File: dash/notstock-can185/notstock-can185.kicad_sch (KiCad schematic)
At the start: 27 parts, among them J1 OBD 12V GND H L, J2 LCD-1.85 header, U1 LMR16006YDDCR, U2 TJA1051T/3

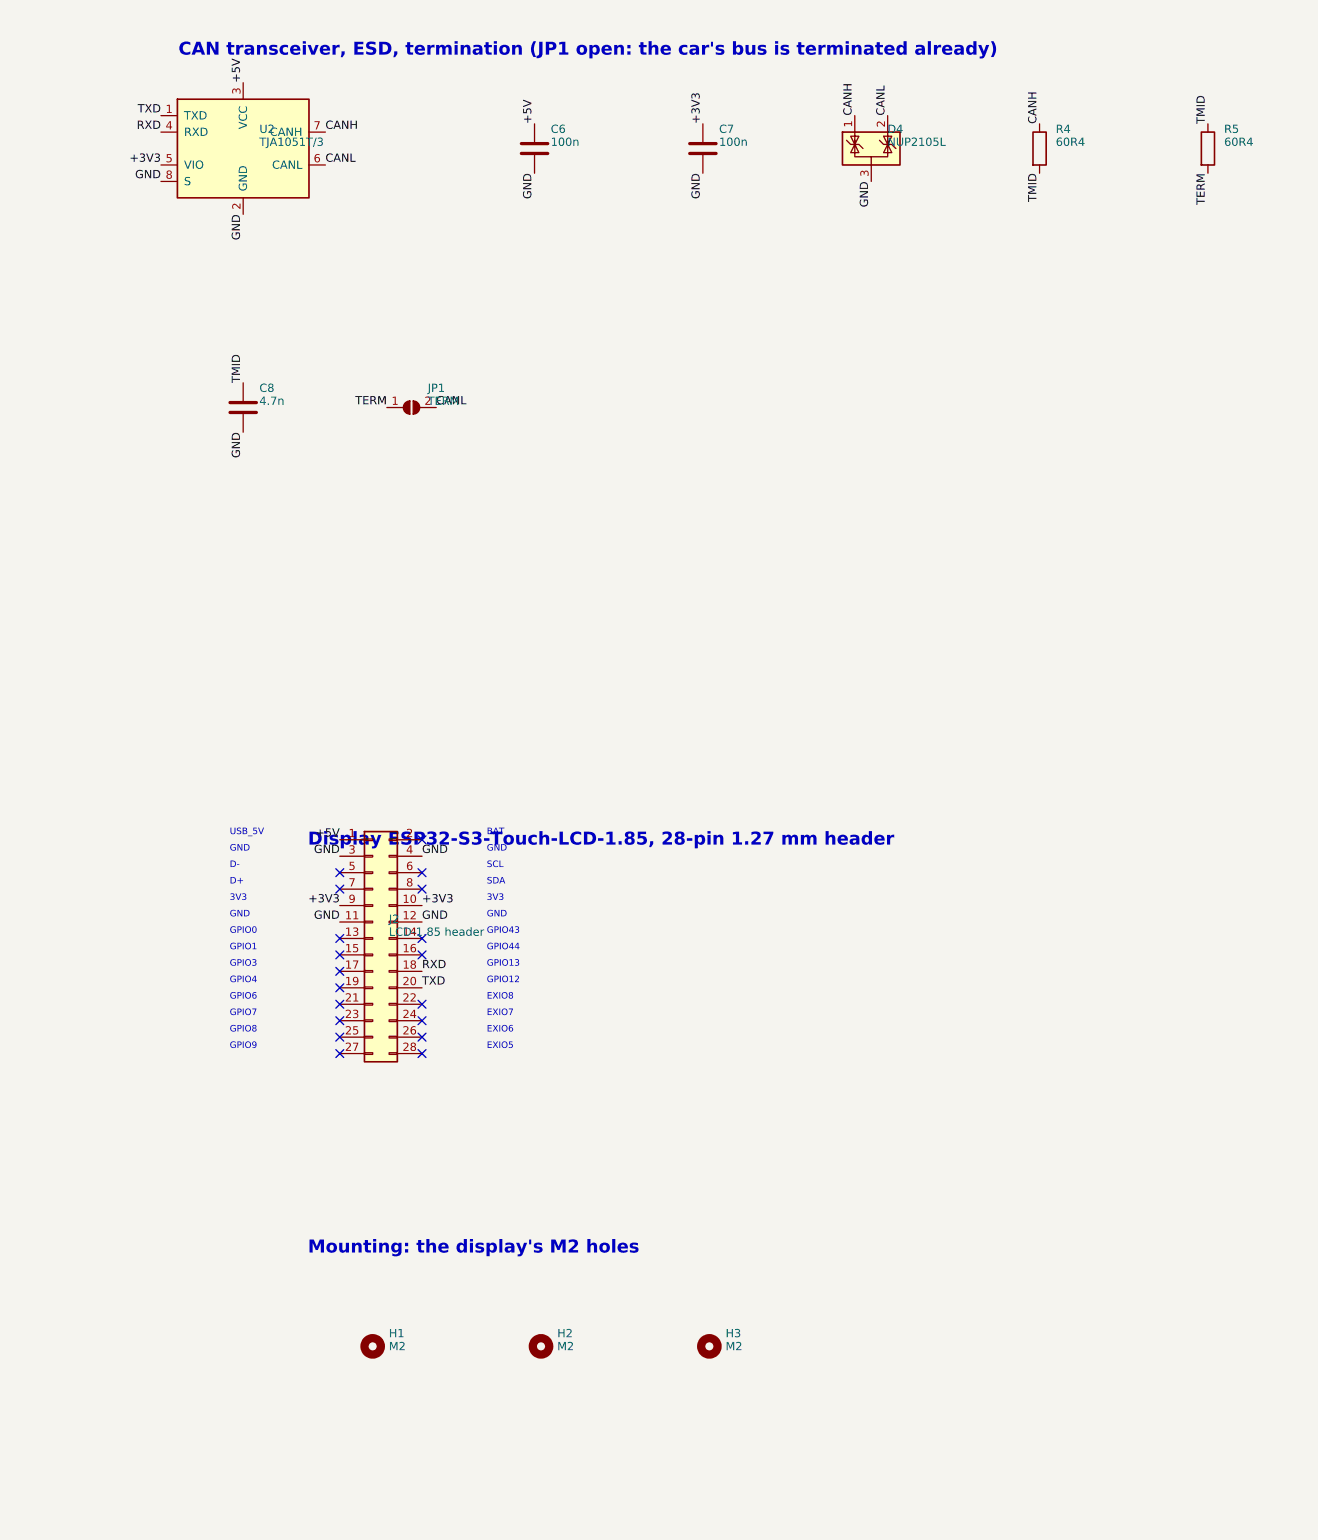
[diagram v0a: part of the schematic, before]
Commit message: CAN 1.85 rev 2: the real ESP32-S3-Touch-LCD-1.85's mechanics and sockets
Waveshare's drawing and schematic of the board (ESP32-S3-LCD-1.85) show
no plug-on header: rev 1 followed the 1.85C, which has one. Now:
Ø48 outline and the three M2 holes from the drawing (DXF), CAN through the
display's 4-pin 1.0 mm UART socket on a 1:1 JST SH cable (GPIO44 TX,
GPIO43 RX, 3V3, GND; 1 k in RXD against the boot ROM's output on
GPIO43), 5 V to the display's USB-C from a USB-C socket on this board.
Edge keepout for the autorouter. DRC clean.

Firmware for the 1.85: CAN on GPIO44/43, the boot loader quiet; the
touch's GPIO1/3 noted as this board's.

Co-Authored-By: Claude Opus 5.5 <noreply@anthropic.com>
Claude-Session: https://claude.ai/code/session_018SKN4tJhAPpVCWtvRZgZpD
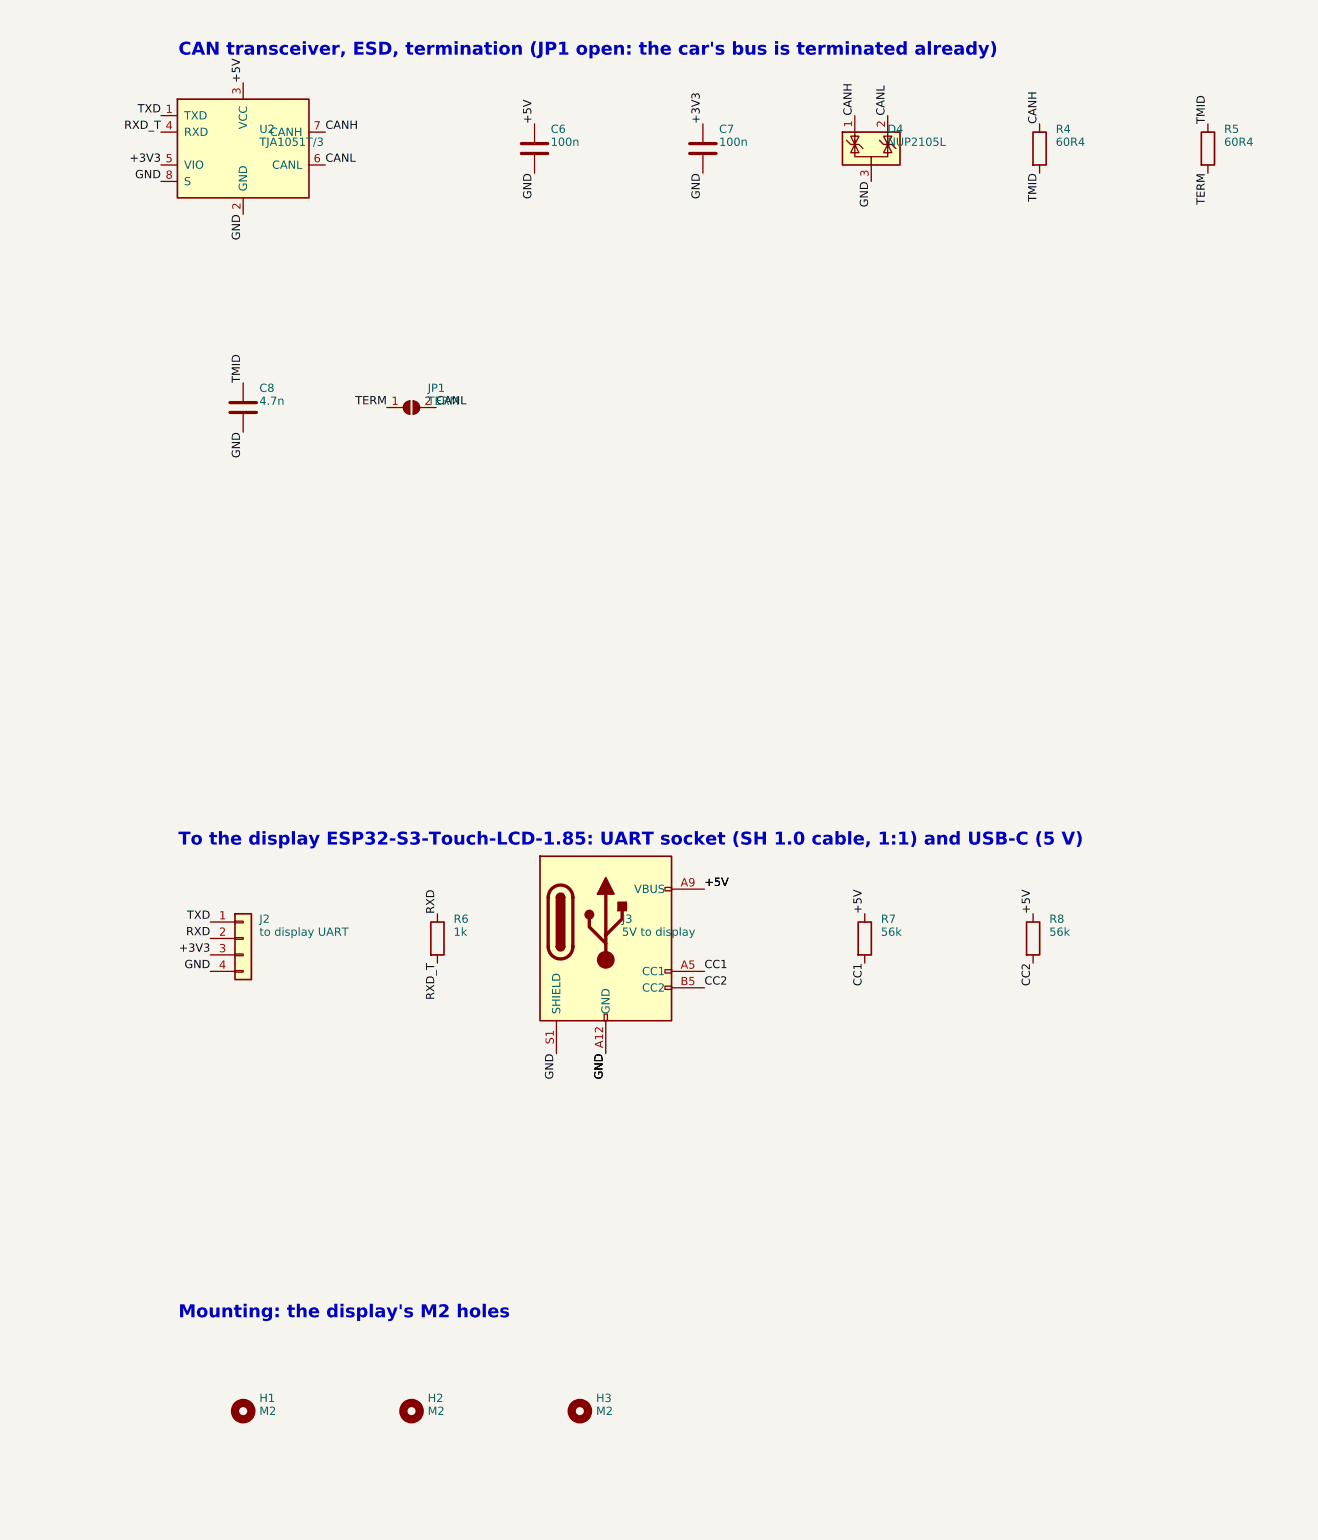
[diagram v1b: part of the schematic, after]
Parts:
- added J3: 5V to display, Connector_USB:USB_C_Receptacle_GCT_USB4125-xx-x_6P_TopMnt_Horizontal, symbol Connector:USB_C_Receptacle_PowerOnly_6P
- added R6: 1k, Resistor_SMD:R_0603_1608Metric, symbol Device:R
- added R7, R8: 56k, Resistor_SMD:R_0603_1608Metric, symbol Device:R
- J2: value LCD-1.85 header -> to display UART; footprint Connector_PinSocket_1.27mm:PinSocket_2x14_P1.27mm_Vertical -> Connector_JST:JST_SH_BM04B-SRSS-TB_1x04-1MP_P1.00mm_Vertical; symbol Connector_Generic:Conn_02x14_Odd_Even -> Connector_Generic:Conn_01x04
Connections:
- net +3V3: now also J2.3 (Pin_3); no longer J2.10 (Pin_10), J2.9 (Pin_9)
- net +5V: now also J3.A9 (VBUS), J3.B9 (VBUS), R7.1, R8.1; no longer J2.1 (Pin_1)
- net GND: now also J3.A12 (GND), J3.B12 (GND), J3.S1 (SHIELD); no longer J2.11 (Pin_11), J2.12 (Pin_12), J2.3 (Pin_3)
- net RXD: now also J2.2 (Pin_2), R6.1; no longer J2.18 (Pin_18), U2.4 (RXD)
- net TXD: now also J2.1 (Pin_1); no longer J2.20 (Pin_20)
- new net CC1: J3.A5 (CC1), R7.2
- new net CC2: J3.B5 (CC2), R8.2
- new net RXD_T: R6.2, U2.4 (RXD)
- no-connect marks 19 -> 0
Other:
- note added: "To the display ESP32-S3-Touch-LCD-1.85: UART socket (SH 1.0 cable, 1:1) and USB-C (5 V)"
- note removed: "3V3"
- note removed: "BAT"
- note removed: "D+"
- note removed: "D-"
- note removed: "Display ESP32-S3-Touch-LCD-1.85, 28-pin 1.27 mm header"
- note removed: "EXIO5"
- note removed: "EXIO6"
- note removed: "EXIO7"
- note removed: "EXIO8"
- note removed: "GND"
- note removed: "GPIO0"
- note removed: "GPIO1"
- note removed: "GPIO12"
- note removed: "GPIO13"
- note removed: "GPIO3"
- note removed: "GPIO4"
- note removed: "GPIO43"
- note removed: "GPIO44"
- note removed: "GPIO6"
- note removed: "GPIO7"
- note removed: "GPIO8"
- note removed: "GPIO9"
- note removed: "SCL"
- note removed: "SDA"
- note removed: "USB_5V"
- moved on the sheet: H1, H2, H3

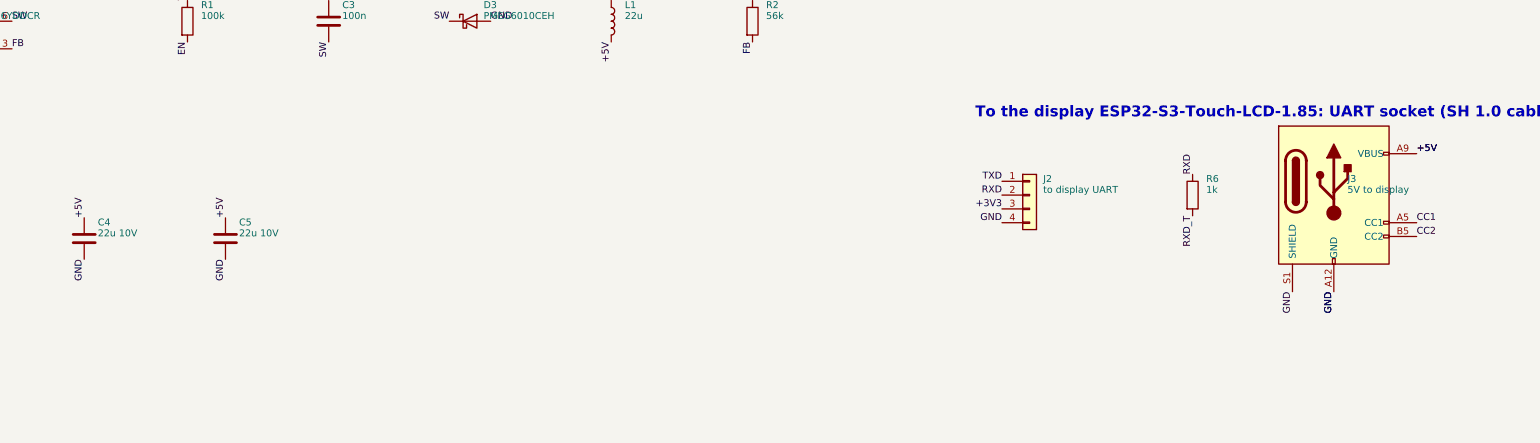
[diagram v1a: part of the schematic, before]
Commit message: CAN 1.85 rev 3: ready for JLCPCB assembly
LCSC numbers for every part (looked up on LCSC/JLCPCB), in design.py,
the schematic (LCSC and MPN fields), the footprints and fab/bom.csv;
values matched to the parts (22 uF 16 V). J3 now the HRO TYPE-C-31-M-12
JLCPCB stocks; its two VBUS pad pairs joined by a short bridge
underneath before autorouting (and routes coming back from the session
not duplicated). Silkscreen past the edge trimmed. DRC clean.

Co-Authored-By: Claude Opus 5.5 <noreply@anthropic.com>
Claude-Session: https://claude.ai/code/session_018SKN4tJhAPpVCWtvRZgZpD
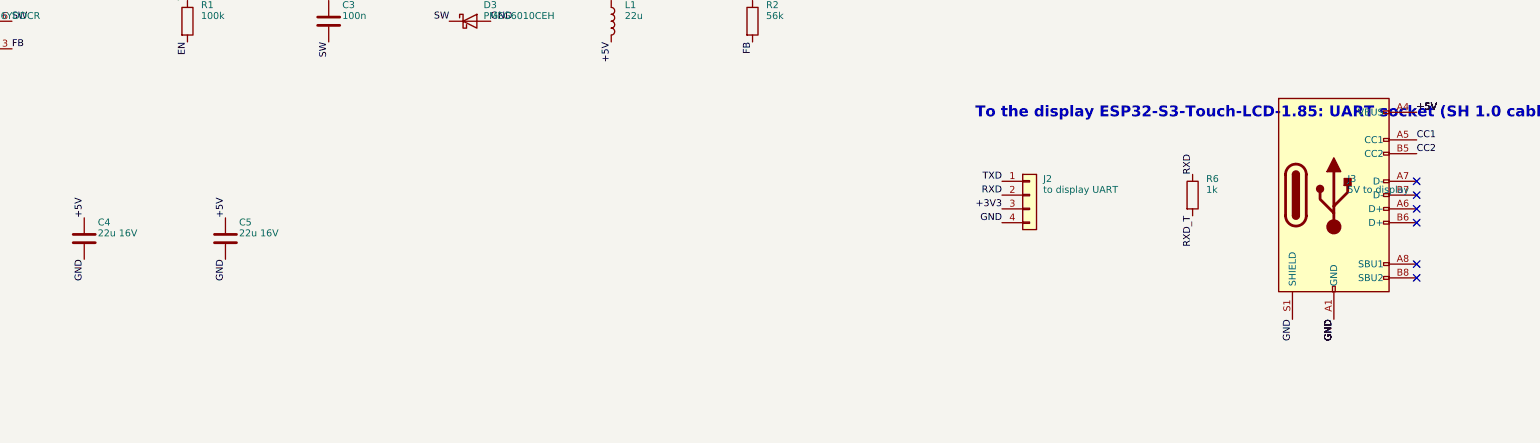
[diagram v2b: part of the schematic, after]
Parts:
- C1: LCSC (none) -> C77096; MPN (none) -> Murata GRM31CR71H475KA12L (4.7 uF 50 V X7R 1206)
- C2, C3, C6, C7: LCSC (none) -> C14663; MPN (none) -> YAGEO CC0603KRX7R9BB104 (100 nF 50 V)
- C4, C5: value 22u 10V -> 22u 16V; LCSC (none) -> C90146; MPN (none) -> Samsung CL31A226KOHNNNE (22 uF 16 V X5R 1206)
- C8: LCSC (none) -> C53987; MPN (none) -> FH 0603B472K500NT (4.7 nF 50 V X7R)
- D1: LCSC (none) -> C2758574; MPN (none) -> UMW SS16 (60 V 1 A)
- D2: LCSC (none) -> C383018; MPN (none) -> SMAJ26A
- D3: LCSC (none) -> C110797; MPN (none) -> Nexperia PMEG6010CEH,115
- D4: LCSC (none) -> C14486; MPN (none) -> onsemi NUP2105LT1G
- F1: LCSC (none) -> C12559; MPN (none) -> RUILON SMD1812P050TF/30 (0.5 A, 30 V)
- H1, H2, H3: MPN (none) -> M2
- J1: LCSC (none) -> C160354; MPN (none) -> JST B4B-PH-SM4-TB(LF)(SN)
- J2: LCSC (none) -> C160390; MPN (none) -> JST BM04B-SRSS-TB(LF)(SN)
- J3: footprint Connector_USB:USB_C_Receptacle_GCT_USB4125-xx-x_6P_TopMnt_Horizontal -> Connector_USB:USB_C_Receptacle_HRO_TYPE-C-31-M-12; symbol Connector:USB_C_Receptacle_PowerOnly_6P -> Connector:USB_C_Receptacle_USB2.0_16P; LCSC (none) -> C165948; MPN (none) -> HRO TYPE-C-31-M-12 (USB-C, data pins open)
- JP1: MPN (none) -> (solder bridge)
- L1: LCSC (none) -> C88254; MPN (none) -> Sunlord SWPA4026S220MT (22 uH)
- R1: LCSC (none) -> C25803; MPN (none) -> UNI-ROYAL 0603WAF1003T5E (100 k 1%)
- R2, R7, R8: LCSC (none) -> C23206; MPN (none) -> UNI-ROYAL 0603WAF5602T5E (56 k 1%)
- R3: LCSC (none) -> C25804; MPN (none) -> UNI-ROYAL 0603WAF1002T5E (10 k 1%)
- R4, R5: LCSC (none) -> C273897; MPN (none) -> YAGEO RC0805FR-0760R4L (60.4 R 1%)
- R6: LCSC (none) -> C21190; MPN (none) -> UNI-ROYAL 0603WAF1001T5E (1 k 1%)
- U1: LCSC (none) -> C290195; MPN (none) -> TI LMR16006YDDCR
- U2: LCSC (none) -> C38695; MPN (none) -> NXP TJA1051T/3/1J
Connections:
- net +5V: now also J3.A4 (VBUS), J3.B4 (VBUS)
- net GND: now also J3.A1 (GND), J3.B1 (GND)
- no-connect marks 0 -> 6

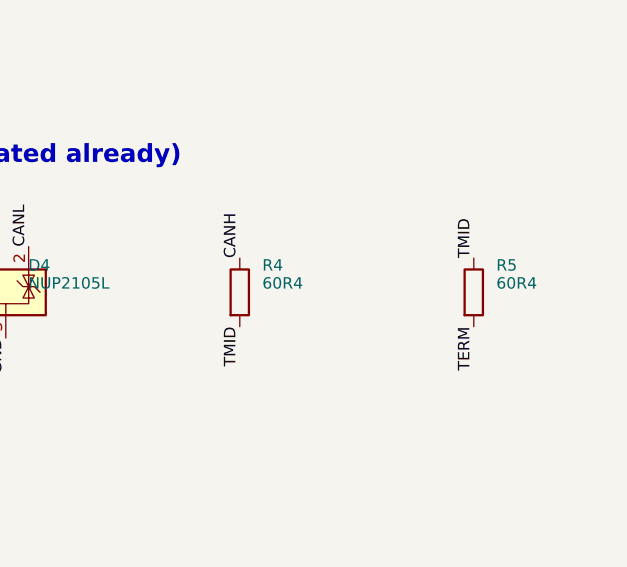
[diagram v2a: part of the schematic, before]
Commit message: CAN 1.85: R4/R5 62 R Walsin C5805111 (60.4 R out of stock)
Co-Authored-By: Claude Opus 5.5 <noreply@anthropic.com>
Claude-Session: https://claude.ai/code/session_018SKN4tJhAPpVCWtvRZgZpD
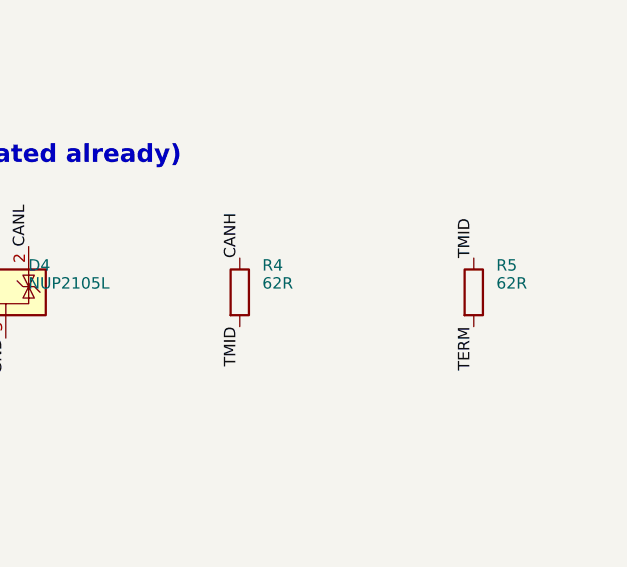
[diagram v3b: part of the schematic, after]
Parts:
- R4, R5: value 60R4 -> 62R; LCSC C273897 -> C5805111; MPN YAGEO RC0805FR-0760R4L (60.4 R 1%) -> Walsin MR08X62R0FTL (62 R 1%)
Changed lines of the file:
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@@
     (property "Reference" "R4" (at 355.5 47 0)
       (effects (font (size 1.27 1.27)) (justify left)))
-    (property "Value" "60R4" (at 355.5 49 0)
+    (property "Value" "62R" (at 355.5 49 0)
       (effects (font (size 1.27 1.27)) (justify left)))
     (property "Footprint" "Resistor_SMD:R_0805_2012Metric" (at 353 50 0)
@@
     (property "Datasheet" "~" (at 353 50 0)
       (effects (font (size 1.27 1.27)) hide))
-    (property "LCSC" "C273897" (at 353 50 0)
+    (property "LCSC" "C5805111" (at 353 50 0)
       (effects (font (size 1.27 1.27)) hide))
-    (property "MPN" "YAGEO RC0805FR-0760R4L (60.4 R 1%)" (at 353 50 0)
+    (property "MPN" "Walsin MR08X62R0FTL (62 R 1%)" (at 353 50 0)
       (effects (font (size 1.27 1.27)) hide))
     (pin "1")
@@
     (property "Reference" "R5" (at 381.5 47 0)
       (effects (font (size 1.27 1.27)) (justify left)))
-    (property "Value" "60R4" (at 381.5 49 0)
+    (property "Value" "62R" (at 381.5 49 0)
       (effects (font (size 1.27 1.27)) (justify left)))
     (property "Footprint" "Resistor_SMD:R_0805_2012Metric" (at 379 50 0)
@@
     (property "Datasheet" "~" (at 379 50 0)
       (effects (font (size 1.27 1.27)) hide))
-    (property "LCSC" "C273897" (at 379 50 0)
+    (property "LCSC" "C5805111" (at 379 50 0)
       (effects (font (size 1.27 1.27)) hide))
-    (property "MPN" "YAGEO RC0805FR-0760R4L (60.4 R 1%)" (at 379 50 0)
+    (property "MPN" "Walsin MR08X62R0FTL (62 R 1%)" (at 379 50 0)
       (effects (font (size 1.27 1.27)) hide))
     (pin "1")
